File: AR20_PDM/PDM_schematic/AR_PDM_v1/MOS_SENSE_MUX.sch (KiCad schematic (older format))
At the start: 14 parts

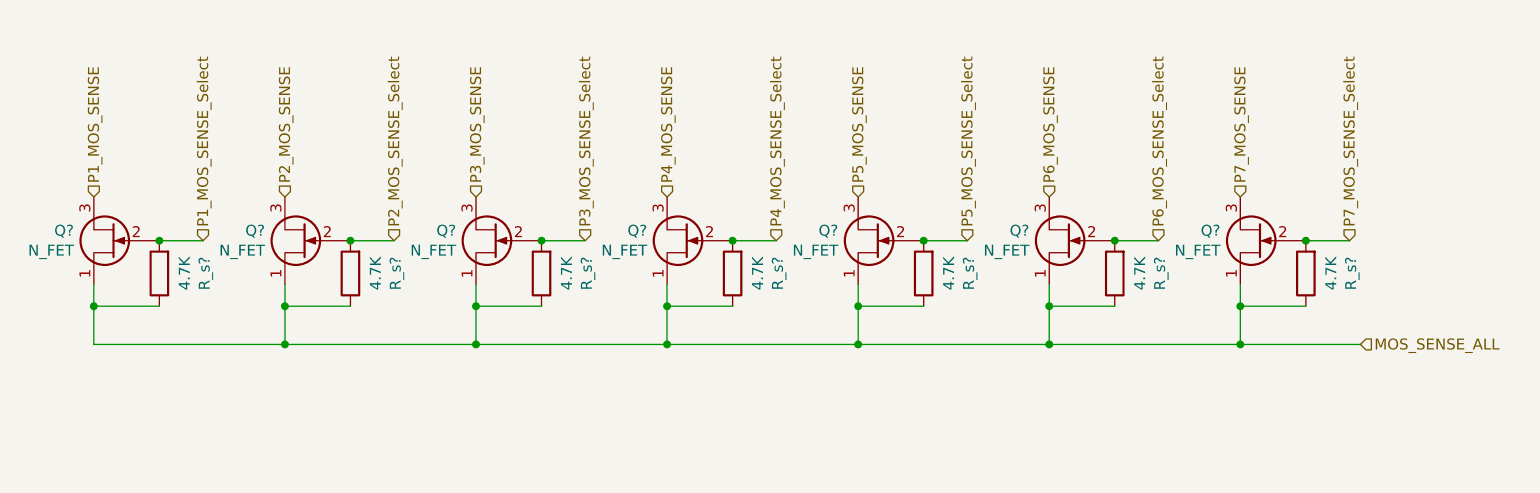
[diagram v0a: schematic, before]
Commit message: Fixed issues, controlled components, BOM, see discription
- added acm symbol
- fixed wrongly faced P-mosfets
- I/O expander now sinks led instead of source
- Bill of material mostly done
- Correct address for INA233 chips.
- Now 4 diodes serves as flyback for all mosfets
- Corrected naming scheme for compmonents (everything is not fixed yet)
- Fixed some labels
- altso some minor changes
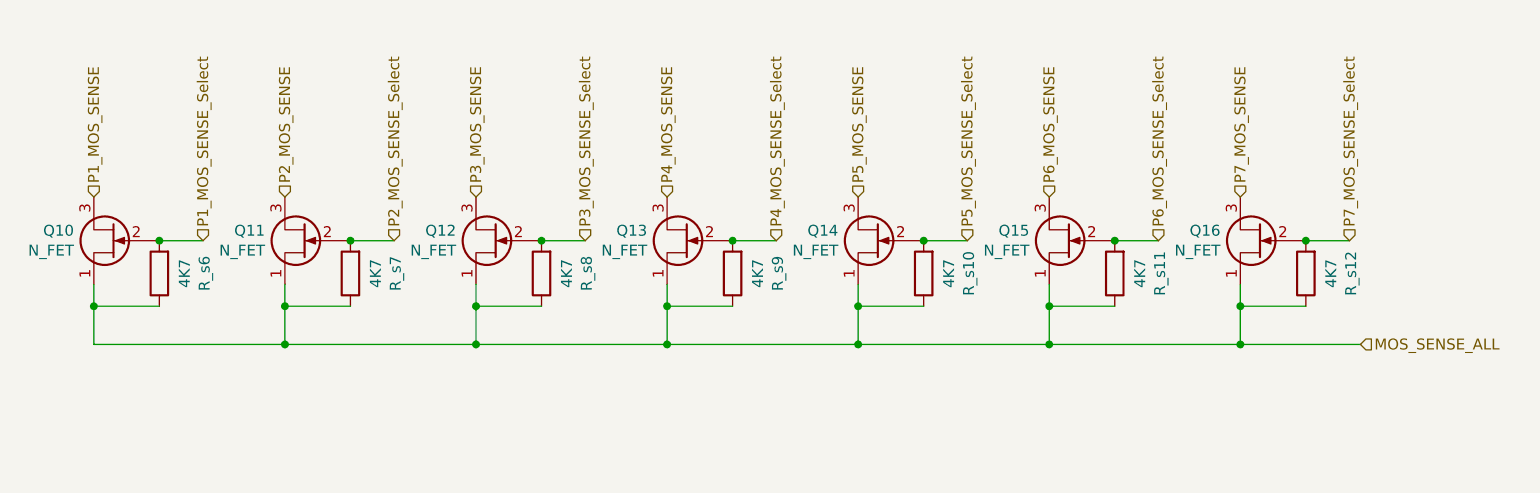
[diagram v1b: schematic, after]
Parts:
- R_s10, R_s11, R_s12, R_s6, R_s7, R_s8, R_s9: renamed from R_s?; value 4.7K -> 4K7
- gave numbers to parts that had none: 7
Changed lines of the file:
@@
 $Descr A4 11693 8268
 encoding utf-8
-Sheet 12 13
+Sheet 11 13
 Title ""
 Date ""
@@
 P 1100 2025
 AR Path="/5DA8920B/5E25DB26" Ref="Q?"  Part="1"
-AR Path="/5E2546F2/5E25DB26" Ref="Q?"  Part="1"
-F 0 "Q?" H 1291 1979 50  0000 L CNN
+AR Path="/5E2546F2/5E25DB26" Ref="Q10"  Part="1"
+F 0 "Q10" H 1291 1979 50  0000 L CNN
 F 1 "N_FET" H 1291 2070 50  0000 L CNN
 F 2 "" H 1300 2125 50  0001 C CNN
@@
 AR Path="/5DA89415/5E25DB2C" Ref="R_s?"  Part="1"
 AR Path="/5DA8920B/5E25DB2C" Ref="R_s?"  Part="1"
-AR Path="/5E2546F2/5E25DB2C" Ref="R_s?"  Part="1"
-F 0 "R_s?" V 1093 2175 50  0000 C CNN
-F 1 "4.7K" V 1184 2175 50  0000 C CNN
+AR Path="/5E2546F2/5E25DB2C" Ref="R_s6"  Part="1"
+F 0 "R_s6" V 1093 2175 50  0000 C CNN
+F 1 "4K7" V 1184 2175 50  0000 C CNN
 F 2 "" V 1230 2175 50  0001 C CNN
 F 3 "~" H 1300 2175 50  0001 C CNN
@@
 P 1975 2025
 AR Path="/5DA8920B/5E263276" Ref="Q?"  Part="1"
-AR Path="/5E2546F2/5E263276" Ref="Q?"  Part="1"
-F 0 "Q?" H 2166 1979 50  0000 L CNN
+AR Path="/5E2546F2/5E263276" Ref="Q11"  Part="1"
+F 0 "Q11" H 2166 1979 50  0000 L CNN
 F 1 "N_FET" H 2166 2070 50  0000 L CNN
 F 2 "" H 2175 2125 50  0001 C CNN
@@
 AR Path="/5DA89415/5E26327C" Ref="R_s?"  Part="1"
 AR Path="/5DA8920B/5E26327C" Ref="R_s?"  Part="1"
-AR Path="/5E2546F2/5E26327C" Ref="R_s?"  Part="1"
-F 0 "R_s?" V 1968 2175 50  0000 C CNN
-F 1 "4.7K" V 2059 2175 50  0000 C CNN
+AR Path="/5E2546F2/5E26327C" Ref="R_s7"  Part="1"
+F 0 "R_s7" V 1968 2175 50  0000 C CNN
+F 1 "4K7" V 2059 2175 50  0000 C CNN
 F 2 "" V 2105 2175 50  0001 C CNN
 F 3 "~" H 2175 2175 50  0001 C CNN
@@
 P 2850 2025
 AR Path="/5DA8920B/5E263C27" Ref="Q?"  Part="1"
-AR Path="/5E2546F2/5E263C27" Ref="Q?"  Part="1"
-F 0 "Q?" H 3041 1979 50  0000 L CNN
+AR Path="/5E2546F2/5E263C27" Ref="Q12"  Part="1"
+F 0 "Q12" H 3041 1979 50  0000 L CNN
 F 1 "N_FET" H 3041 2070 50  0000 L CNN
 F 2 "" H 3050 2125 50  0001 C CNN
@@
 AR Path="/5DA89415/5E263C2D" Ref="R_s?"  Part="1"
 AR Path="/5DA8920B/5E263C2D" Ref="R_s?"  Part="1"
-AR Path="/5E2546F2/5E263C2D" Ref="R_s?"  Part="1"
-F 0 "R_s?" V 2843 2175 50  0000 C CNN
-F 1 "4.7K" V 2934 2175 50  0000 C CNN
+AR Path="/5E2546F2/5E263C2D" Ref="R_s8"  Part="1"
+F 0 "R_s8" V 2843 2175 50  0000 C CNN
+F 1 "4K7" V 2934 2175 50  0000 C CNN
 F 2 "" V 2980 2175 50  0001 C CNN
 F 3 "~" H 3050 2175 50  0001 C CNN
@@
 P 3725 2025
 AR Path="/5DA8920B/5E264DAD" Ref="Q?"  Part="1"
-AR Path="/5E2546F2/5E264DAD" Ref="Q?"  Part="1"
-F 0 "Q?" H 3916 1979 50  0000 L CNN
+AR Path="/5E2546F2/5E264DAD" Ref="Q13"  Part="1"
+F 0 "Q13" H 3916 1979 50  0000 L CNN
 F 1 "N_FET" H 3916 2070 50  0000 L CNN
 F 2 "" H 3925 2125 50  0001 C CNN
@@
 AR Path="/5DA89415/5E264DB3" Ref="R_s?"  Part="1"
 AR Path="/5DA8920B/5E264DB3" Ref="R_s?"  Part="1"
-AR Path="/5E2546F2/5E264DB3" Ref="R_s?"  Part="1"
-F 0 "R_s?" V 3718 2175 50  0000 C CNN
-F 1 "4.7K" V 3809 2175 50  0000 C CNN
+AR Path="/5E2546F2/5E264DB3" Ref="R_s9"  Part="1"
+F 0 "R_s9" V 3718 2175 50  0000 C CNN
+F 1 "4K7" V 3809 2175 50  0000 C CNN
 F 2 "" V 3855 2175 50  0001 C CNN
 F 3 "~" H 3925 2175 50  0001 C CNN
@@
 P 4600 2025
 AR Path="/5DA8920B/5E266900" Ref="Q?"  Part="1"
-AR Path="/5E2546F2/5E266900" Ref="Q?"  Part="1"
-F 0 "Q?" H 4791 1979 50  0000 L CNN
+AR Path="/5E2546F2/5E266900" Ref="Q14"  Part="1"
+F 0 "Q14" H 4791 1979 50  0000 L CNN
 F 1 "N_FET" H 4791 2070 50  0000 L CNN
 F 2 "" H 4800 2125 50  0001 C CNN
@@
 AR Path="/5DA89415/5E266906" Ref="R_s?"  Part="1"
 AR Path="/5DA8920B/5E266906" Ref="R_s?"  Part="1"
-AR Path="/5E2546F2/5E266906" Ref="R_s?"  Part="1"
-F 0 "R_s?" V 4593 2175 50  0000 C CNN
-F 1 "4.7K" V 4684 2175 50  0000 C CNN
+AR Path="/5E2546F2/5E266906" Ref="R_s10"  Part="1"
+F 0 "R_s10" V 4593 2175 50  0000 C CNN
+F 1 "4K7" V 4684 2175 50  0000 C CNN
 F 2 "" V 4730 2175 50  0001 C CNN
 F 3 "~" H 4800 2175 50  0001 C CNN
@@
 P 5475 2025
 AR Path="/5DA8920B/5E26A04E" Ref="Q?"  Part="1"
-AR Path="/5E2546F2/5E26A04E" Ref="Q?"  Part="1"
-F 0 "Q?" H 5666 1979 50  0000 L CNN
+AR Path="/5E2546F2/5E26A04E" Ref="Q15"  Part="1"
+F 0 "Q15" H 5666 1979 50  0000 L CNN
 F 1 "N_FET" H 5666 2070 50  0000 L CNN
 F 2 "" H 5675 2125 50  0001 C CNN
@@
 AR Path="/5DA89415/5E26A054" Ref="R_s?"  Part="1"
 AR Path="/5DA8920B/5E26A054" Ref="R_s?"  Part="1"
-AR Path="/5E2546F2/5E26A054" Ref="R_s?"  Part="1"
-F 0 "R_s?" V 5468 2175 50  0000 C CNN
-F 1 "4.7K" V 5559 2175 50  0000 C CNN
+AR Path="/5E2546F2/5E26A054" Ref="R_s11"  Part="1"
+F 0 "R_s11" V 5468 2175 50  0000 C CNN
+F 1 "4K7" V 5559 2175 50  0000 C CNN
 F 2 "" V 5605 2175 50  0001 C CNN
 F 3 "~" H 5675 2175 50  0001 C CNN
@@
 P 6350 2025
 AR Path="/5DA8920B/5E26B53D" Ref="Q?"  Part="1"
-AR Path="/5E2546F2/5E26B53D" Ref="Q?"  Part="1"
-F 0 "Q?" H 6541 1979 50  0000 L CNN
+AR Path="/5E2546F2/5E26B53D" Ref="Q16"  Part="1"
+F 0 "Q16" H 6541 1979 50  0000 L CNN
 F 1 "N_FET" H 6541 2070 50  0000 L CNN
 F 2 "" H 6550 2125 50  0001 C CNN
@@
 AR Path="/5DA89415/5E26B543" Ref="R_s?"  Part="1"
 AR Path="/5DA8920B/5E26B543" Ref="R_s?"  Part="1"
-AR Path="/5E2546F2/5E26B543" Ref="R_s?"  Part="1"
-F 0 "R_s?" V 6343 2175 50  0000 C CNN
-F 1 "4.7K" V 6434 2175 50  0000 C CNN
+AR Path="/5E2546F2/5E26B543" Ref="R_s12"  Part="1"
+F 0 "R_s12" V 6343 2175 50  0000 C CNN
+F 1 "4K7" V 6434 2175 50  0000 C CNN
 F 2 "" V 6480 2175 50  0001 C CNN
 F 3 "~" H 6550 2175 50  0001 C CNN

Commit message: PCB design, and issue fixing, work in progress
- Error fixed: Mux mosfet resistor change to ground
- Open drain output added on phase 6, for engine blipping purpose
- Most of pcb symbols and footprints are finished, including main connector
- PCB is change from 1oz to 2oz copper layer, for easier routing.
- Basic Draft of pcb is done, for now.
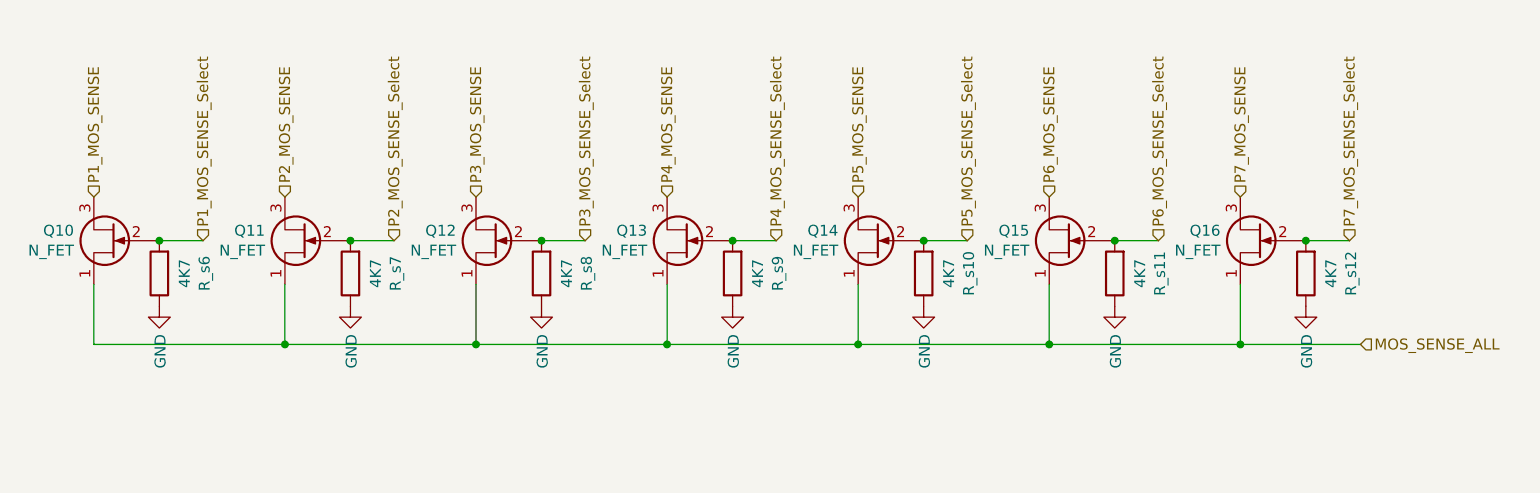
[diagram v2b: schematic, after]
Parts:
- Q10, Q11, Q12, Q13, Q14, Q15, Q16: footprint (none) -> Package_TO_SOT_SMD:SOT-23
- R_s10, R_s11, R_s12, R_s6, R_s7, R_s8, R_s9: footprint (none) -> Resistor_SMD:R_0603_1608Metric
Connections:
- net MOS_SENSE_ALL: no longer R_s10.1, R_s11.1, R_s12.1, R_s6.1, R_s7.1, R_s8.1, R_s9.1
- new net GND: R_s10.1, R_s11.1, R_s12.1, R_s6.1, R_s7.1, R_s8.1, R_s9.1

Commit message: Alpha version DONE! - Gerber files generated
- Tweeked
- checked and re cheked
- added all missing components
- Created a really nice silkscreen
- Ready To Test
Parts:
- renumbered Q11 to Q10, Q12 to Q11, Q13 to Q12, Q14 to Q13, Q15 to Q14, Q16 to Q15, Q10 to Q9, R_s6 to R40, R_s7 to R41, R_s8 to R42, R_s9 to R43, R_s11 to R44, R_s12 to R45, R_s10 to R_s1
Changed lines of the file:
@@
 $Descr A4 11693 8268
 encoding utf-8
-Sheet 10 13
+Sheet 9 13
 Title ""
 Date ""
@@
 P 1100 2025
 AR Path="/5DA8920B/5E25DB26" Ref="Q?"  Part="1"
-AR Path="/5E2546F2/5E25DB26" Ref="Q10"  Part="1"
-F 0 "Q10" H 1291 1979 50  0000 L CNN
+AR Path="/5E2546F2/5E25DB26" Ref="Q9"  Part="1"
+F 0 "Q9" H 1291 1979 50  0000 L CNN
 F 1 "N_FET" H 1291 2070 50  0000 L CNN
 F 2 "Package_TO_SOT_SMD:SOT-23" H 1300 2125 50  0001 C CNN
@@
 $EndComp
 $Comp
-L AR20_PDM_v1-rescue:R-Device R_s?
+L AR20_PDM_v1-rescue:R-Device R?
 U 1 1 5E25DB2C
 P 1300 2175
-AR Path="/5DA89415/5E25DB2C" Ref="R_s?"  Part="1"
-AR Path="/5DA8920B/5E25DB2C" Ref="R_s?"  Part="1"
-AR Path="/5E2546F2/5E25DB2C" Ref="R_s6"  Part="1"
-F 0 "R_s6" V 1093 2175 50  0000 C CNN
+AR Path="/5DA89415/5E25DB2C" Ref="R?"  Part="1"
+AR Path="/5DA8920B/5E25DB2C" Ref="R?"  Part="1"
+AR Path="/5E2546F2/5E25DB2C" Ref="R40"  Part="1"
+F 0 "R40" V 1093 2175 50  0000 C CNN
 F 1 "4K7" V 1184 2175 50  0000 C CNN
 F 2 "Resistor_SMD:R_0603_1608Metric" V 1230 2175 50  0001 C CNN
@@
 P 1975 2025
 AR Path="/5DA8920B/5E263276" Ref="Q?"  Part="1"
-AR Path="/5E2546F2/5E263276" Ref="Q11"  Part="1"
-F 0 "Q11" H 2166 1979 50  0000 L CNN
+AR Path="/5E2546F2/5E263276" Ref="Q10"  Part="1"
+F 0 "Q10" H 2166 1979 50  0000 L CNN
 F 1 "N_FET" H 2166 2070 50  0000 L CNN
 F 2 "Package_TO_SOT_SMD:SOT-23" H 2175 2125 50  0001 C CNN
@@
 $EndComp
 $Comp
-L AR20_PDM_v1-rescue:R-Device R_s?
+L AR20_PDM_v1-rescue:R-Device R?
 U 1 1 5E26327C
 P 2175 2175
-AR Path="/5DA89415/5E26327C" Ref="R_s?"  Part="1"
-AR Path="/5DA8920B/5E26327C" Ref="R_s?"  Part="1"
-AR Path="/5E2546F2/5E26327C" Ref="R_s7"  Part="1"
-F 0 "R_s7" V 1968 2175 50  0000 C CNN
+AR Path="/5DA89415/5E26327C" Ref="R?"  Part="1"
+AR Path="/5DA8920B/5E26327C" Ref="R?"  Part="1"
+AR Path="/5E2546F2/5E26327C" Ref="R41"  Part="1"
+F 0 "R41" V 1968 2175 50  0000 C CNN
 F 1 "4K7" V 2059 2175 50  0000 C CNN
 F 2 "Resistor_SMD:R_0603_1608Metric" V 2105 2175 50  0001 C CNN
@@
 P 2850 2025
 AR Path="/5DA8920B/5E263C27" Ref="Q?"  Part="1"
-AR Path="/5E2546F2/5E263C27" Ref="Q12"  Part="1"
-F 0 "Q12" H 3041 1979 50  0000 L CNN
+AR Path="/5E2546F2/5E263C27" Ref="Q11"  Part="1"
+F 0 "Q11" H 3041 1979 50  0000 L CNN
 F 1 "N_FET" H 3041 2070 50  0000 L CNN
 F 2 "Package_TO_SOT_SMD:SOT-23" H 3050 2125 50  0001 C CNN
@@
 $EndComp
 $Comp
-L AR20_PDM_v1-rescue:R-Device R_s?
+L AR20_PDM_v1-rescue:R-Device R?
 U 1 1 5E263C2D
 P 3050 2175
-AR Path="/5DA89415/5E263C2D" Ref="R_s?"  Part="1"
-AR Path="/5DA8920B/5E263C2D" Ref="R_s?"  Part="1"
-AR Path="/5E2546F2/5E263C2D" Ref="R_s8"  Part="1"
-F 0 "R_s8" V 2843 2175 50  0000 C CNN
+AR Path="/5DA89415/5E263C2D" Ref="R?"  Part="1"
+AR Path="/5DA8920B/5E263C2D" Ref="R?"  Part="1"
+AR Path="/5E2546F2/5E263C2D" Ref="R42"  Part="1"
+F 0 "R42" V 2843 2175 50  0000 C CNN
 F 1 "4K7" V 2934 2175 50  0000 C CNN
 F 2 "Resistor_SMD:R_0603_1608Metric" V 2980 2175 50  0001 C CNN
@@
 P 3725 2025
 AR Path="/5DA8920B/5E264DAD" Ref="Q?"  Part="1"
-AR Path="/5E2546F2/5E264DAD" Ref="Q13"  Part="1"
-F 0 "Q13" H 3916 1979 50  0000 L CNN
+AR Path="/5E2546F2/5E264DAD" Ref="Q12"  Part="1"
+F 0 "Q12" H 3916 1979 50  0000 L CNN
 F 1 "N_FET" H 3916 2070 50  0000 L CNN
 F 2 "Package_TO_SOT_SMD:SOT-23" H 3925 2125 50  0001 C CNN
@@
 $EndComp
 $Comp
-L AR20_PDM_v1-rescue:R-Device R_s?
+L AR20_PDM_v1-rescue:R-Device R?
 U 1 1 5E264DB3
 P 3925 2175
-AR Path="/5DA89415/5E264DB3" Ref="R_s?"  Part="1"
-AR Path="/5DA8920B/5E264DB3" Ref="R_s?"  Part="1"
-AR Path="/5E2546F2/5E264DB3" Ref="R_s9"  Part="1"
-F 0 "R_s9" V 3718 2175 50  0000 C CNN
+AR Path="/5DA89415/5E264DB3" Ref="R?"  Part="1"
+AR Path="/5DA8920B/5E264DB3" Ref="R?"  Part="1"
+AR Path="/5E2546F2/5E264DB3" Ref="R43"  Part="1"
+F 0 "R43" V 3718 2175 50  0000 C CNN
 F 1 "4K7" V 3809 2175 50  0000 C CNN
 F 2 "Resistor_SMD:R_0603_1608Metric" V 3855 2175 50  0001 C CNN
@@
 P 4600 2025
 AR Path="/5DA8920B/5E266900" Ref="Q?"  Part="1"
-AR Path="/5E2546F2/5E266900" Ref="Q14"  Part="1"
-F 0 "Q14" H 4791 1979 50  0000 L CNN
+AR Path="/5E2546F2/5E266900" Ref="Q13"  Part="1"
+F 0 "Q13" H 4791 1979 50  0000 L CNN
 F 1 "N_FET" H 4791 2070 50  0000 L CNN
 F 2 "Package_TO_SOT_SMD:SOT-23" H 4800 2125 50  0001 C CNN
@@
 AR Path="/5DA89415/5E266906" Ref="R_s?"  Part="1"
 AR Path="/5DA8920B/5E266906" Ref="R_s?"  Part="1"
-AR Path="/5E2546F2/5E266906" Ref="R_s10"  Part="1"
-F 0 "R_s10" V 4593 2175 50  0000 C CNN
+AR Path="/5E2546F2/5E266906" Ref="R_s1"  Part="1"
+F 0 "R_s1" V 4593 2175 50  0000 C CNN
 F 1 "4K7" V 4684 2175 50  0000 C CNN
 F 2 "Resistor_SMD:R_0603_1608Metric" V 4730 2175 50  0001 C CNN
@@
 P 5475 2025
 AR Path="/5DA8920B/5E26A04E" Ref="Q?"  Part="1"
-AR Path="/5E2546F2/5E26A04E" Ref="Q15"  Part="1"
-F 0 "Q15" H 5666 1979 50  0000 L CNN
+AR Path="/5E2546F2/5E26A04E" Ref="Q14"  Part="1"
+F 0 "Q14" H 5666 1979 50  0000 L CNN
 F 1 "N_FET" H 5666 2070 50  0000 L CNN
 F 2 "Package_TO_SOT_SMD:SOT-23" H 5675 2125 50  0001 C CNN
@@
 $EndComp
 $Comp
-L AR20_PDM_v1-rescue:R-Device R_s?
+L AR20_PDM_v1-rescue:R-Device R?
 U 1 1 5E26A054
 P 5675 2175
-AR Path="/5DA89415/5E26A054" Ref="R_s?"  Part="1"
-AR Path="/5DA8920B/5E26A054" Ref="R_s?"  Part="1"
-AR Path="/5E2546F2/5E26A054" Ref="R_s11"  Part="1"
-F 0 "R_s11" V 5468 2175 50  0000 C CNN
+AR Path="/5DA89415/5E26A054" Ref="R?"  Part="1"
+AR Path="/5DA8920B/5E26A054" Ref="R?"  Part="1"
+AR Path="/5E2546F2/5E26A054" Ref="R44"  Part="1"
+F 0 "R44" V 5468 2175 50  0000 C CNN
 F 1 "4K7" V 5559 2175 50  0000 C CNN
 F 2 "Resistor_SMD:R_0603_1608Metric" V 5605 2175 50  0001 C CNN
@@
 P 6350 2025
 AR Path="/5DA8920B/5E26B53D" Ref="Q?"  Part="1"
-AR Path="/5E2546F2/5E26B53D" Ref="Q16"  Part="1"
-F 0 "Q16" H 6541 1979 50  0000 L CNN
+AR Path="/5E2546F2/5E26B53D" Ref="Q15"  Part="1"
+F 0 "Q15" H 6541 1979 50  0000 L CNN
 F 1 "N_FET" H 6541 2070 50  0000 L CNN
 F 2 "Package_TO_SOT_SMD:SOT-23" H 6550 2125 50  0001 C CNN
@@
 $EndComp
 $Comp
-L AR20_PDM_v1-rescue:R-Device R_s?
+L AR20_PDM_v1-rescue:R-Device R?
 U 1 1 5E26B543
 P 6550 2175
-AR Path="/5DA89415/5E26B543" Ref="R_s?"  Part="1"
-AR Path="/5DA8920B/5E26B543" Ref="R_s?"  Part="1"
-AR Path="/5E2546F2/5E26B543" Ref="R_s12"  Part="1"
-F 0 "R_s12" V 6343 2175 50  0000 C CNN
+AR Path="/5DA89415/5E26B543" Ref="R?"  Part="1"
+AR Path="/5DA8920B/5E26B543" Ref="R?"  Part="1"
+AR Path="/5E2546F2/5E26B543" Ref="R45"  Part="1"
+F 0 "R45" V 6343 2175 50  0000 C CNN
 F 1 "4K7" V 6434 2175 50  0000 C CNN
 F 2 "Resistor_SMD:R_0603_1608Metric" V 6480 2175 50  0001 C CNN
@@
 AR Path="/5E10174B/5E26BFFA" Ref="#PWR?"  Part="1"
 AR Path="/5E1AEC18/5E26BFFA" Ref="#PWR?"  Part="1"
-AR Path="/5E2546F2/5E26BFFA" Ref="#PWR0125"  Part="1"
-F 0 "#PWR0125" H 1300 2075 50  0001 C CNN
+AR Path="/5E2546F2/5E26BFFA" Ref="#PWR071"  Part="1"
+F 0 "#PWR071" H 1300 2075 50  0001 C CNN
 F 1 "GND" V 1305 2197 50  0000 R CNN
 F 2 "" H 1300 2325 50  0001 C CNN
@@
 AR Path="/5E10174B/5E26C370" Ref="#PWR?"  Part="1"
 AR Path="/5E1AEC18/5E26C370" Ref="#PWR?"  Part="1"
-AR Path="/5E2546F2/5E26C370" Ref="#PWR0126"  Part="1"
-F 0 "#PWR0126" H 2175 2075 50  0001 C CNN
+AR Path="/5E2546F2/5E26C370" Ref="#PWR072"  Part="1"
+F 0 "#PWR072" H 2175 2075 50  0001 C CNN
 F 1 "GND" V 2180 2197 50  0000 R CNN
 F 2 "" H 2175 2325 50  0001 C CNN
@@
 AR Path="/5E10174B/5E26C812" Ref="#PWR?"  Part="1"
 AR Path="/5E1AEC18/5E26C812" Ref="#PWR?"  Part="1"
-AR Path="/5E2546F2/5E26C812" Ref="#PWR0127"  Part="1"
-F 0 "#PWR0127" H 3050 2075 50  0001 C CNN
+AR Path="/5E2546F2/5E26C812" Ref="#PWR073"  Part="1"
+F 0 "#PWR073" H 3050 2075 50  0001 C CNN
 F 1 "GND" V 3055 2197 50  0000 R CNN
 F 2 "" H 3050 2325 50  0001 C CNN
@@
 AR Path="/5E10174B/5E26CB16" Ref="#PWR?"  Part="1"
 AR Path="/5E1AEC18/5E26CB16" Ref="#PWR?"  Part="1"
-AR Path="/5E2546F2/5E26CB16" Ref="#PWR0128"  Part="1"
-F 0 "#PWR0128" H 3925 2075 50  0001 C CNN
+AR Path="/5E2546F2/5E26CB16" Ref="#PWR074"  Part="1"
+F 0 "#PWR074" H 3925 2075 50  0001 C CNN
 F 1 "GND" V 3930 2197 50  0000 R CNN
 F 2 "" H 3925 2325 50  0001 C CNN
@@
 AR Path="/5E10174B/5E26CF0E" Ref="#PWR?"  Part="1"
 AR Path="/5E1AEC18/5E26CF0E" Ref="#PWR?"  Part="1"
-AR Path="/5E2546F2/5E26CF0E" Ref="#PWR0129"  Part="1"
-F 0 "#PWR0129" H 4800 2075 50  0001 C CNN
+AR Path="/5E2546F2/5E26CF0E" Ref="#PWR075"  Part="1"
+F 0 "#PWR075" H 4800 2075 50  0001 C CNN
 F 1 "GND" V 4805 2197 50  0000 R CNN
 F 2 "" H 4800 2325 50  0001 C CNN
@@
 AR Path="/5E10174B/5E26D297" Ref="#PWR?"  Part="1"
 AR Path="/5E1AEC18/5E26D297" Ref="#PWR?"  Part="1"
-AR Path="/5E2546F2/5E26D297" Ref="#PWR0130"  Part="1"
-F 0 "#PWR0130" H 5675 2075 50  0001 C CNN
+AR Path="/5E2546F2/5E26D297" Ref="#PWR076"  Part="1"
+F 0 "#PWR076" H 5675 2075 50  0001 C CNN
 F 1 "GND" V 5680 2197 50  0000 R CNN
 F 2 "" H 5675 2325 50  0001 C CNN
@@
 AR Path="/5E10174B/5E26D54C" Ref="#PWR?"  Part="1"
 AR Path="/5E1AEC18/5E26D54C" Ref="#PWR?"  Part="1"
-AR Path="/5E2546F2/5E26D54C" Ref="#PWR0131"  Part="1"
-F 0 "#PWR0131" H 6550 2075 50  0001 C CNN
+AR Path="/5E2546F2/5E26D54C" Ref="#PWR077"  Part="1"
+F 0 "#PWR077" H 6550 2075 50  0001 C CNN
 F 1 "GND" V 6555 2197 50  0000 R CNN
 F 2 "" H 6550 2325 50  0001 C CNN
